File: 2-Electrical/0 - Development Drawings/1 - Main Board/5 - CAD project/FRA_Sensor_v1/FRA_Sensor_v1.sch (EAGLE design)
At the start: 213 parts, among them IC1 CP2101, IC2 ADS1115IDGSR, IC3 P82B715DR, IC4 ADS1115IDGSR, IC5 ADS1115IDGSR, IC8 PCA9555PW, IC9 LDK320ADU50R, J2 ETH_CONN, J3 PJ-059A, J5 WM9734TR-ND, J8 1140084168, J9 + G SCL SDA, Q10 FDN306P, Q11 FDN306P, Q12 FDN306P, Q13 FDN306P, Q14 FDN306P, Q15 FDN306P, Q2 FDN306P, Q3 Si2300DS, Q5 FDN306P, Q6 FDN306P, Q7 DNI, Q8 FDN306P, Q9 FDN306P, T1 BC847, T2 BC847, U1 PCA9509DP, U2 ESP-WROOM-32, X1 TB001-500-02BE, Y3 32.768kHz

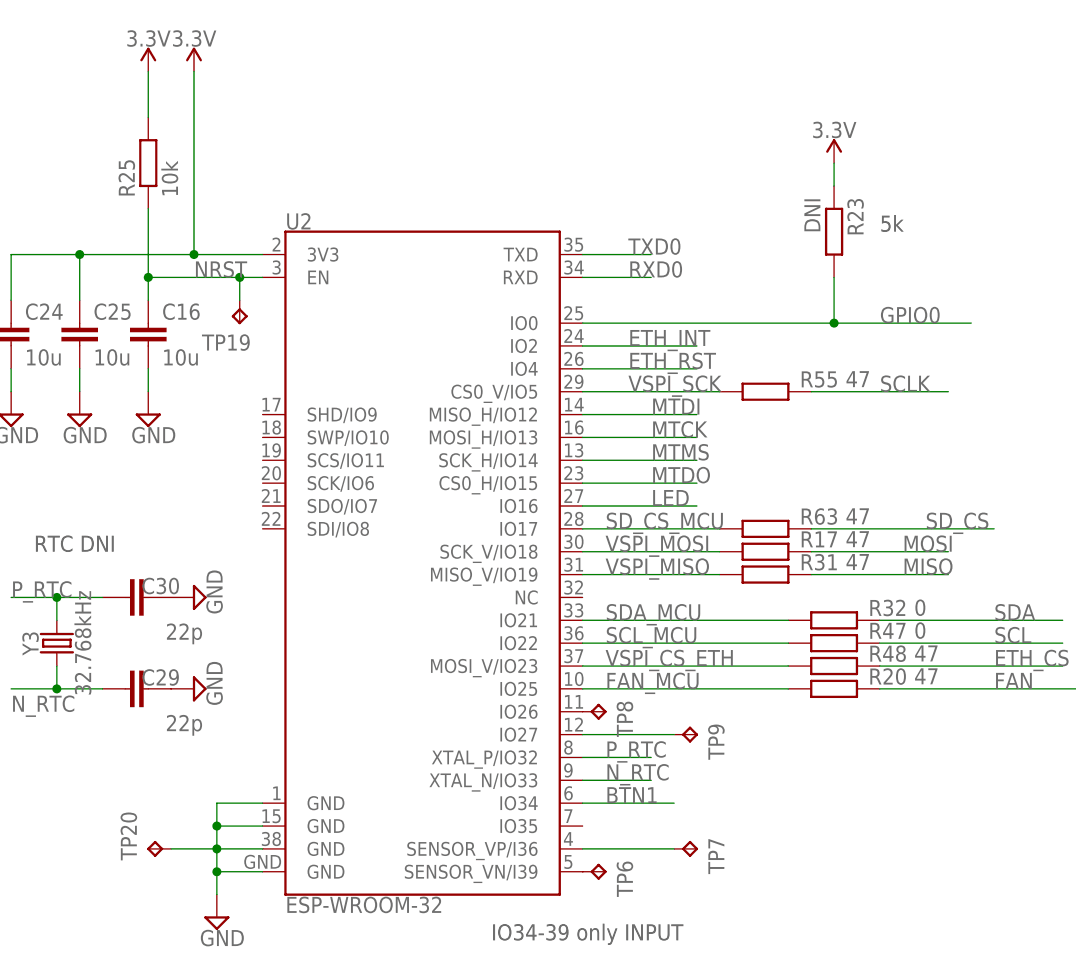
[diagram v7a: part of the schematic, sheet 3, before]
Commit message: error report fixed and sw reset done
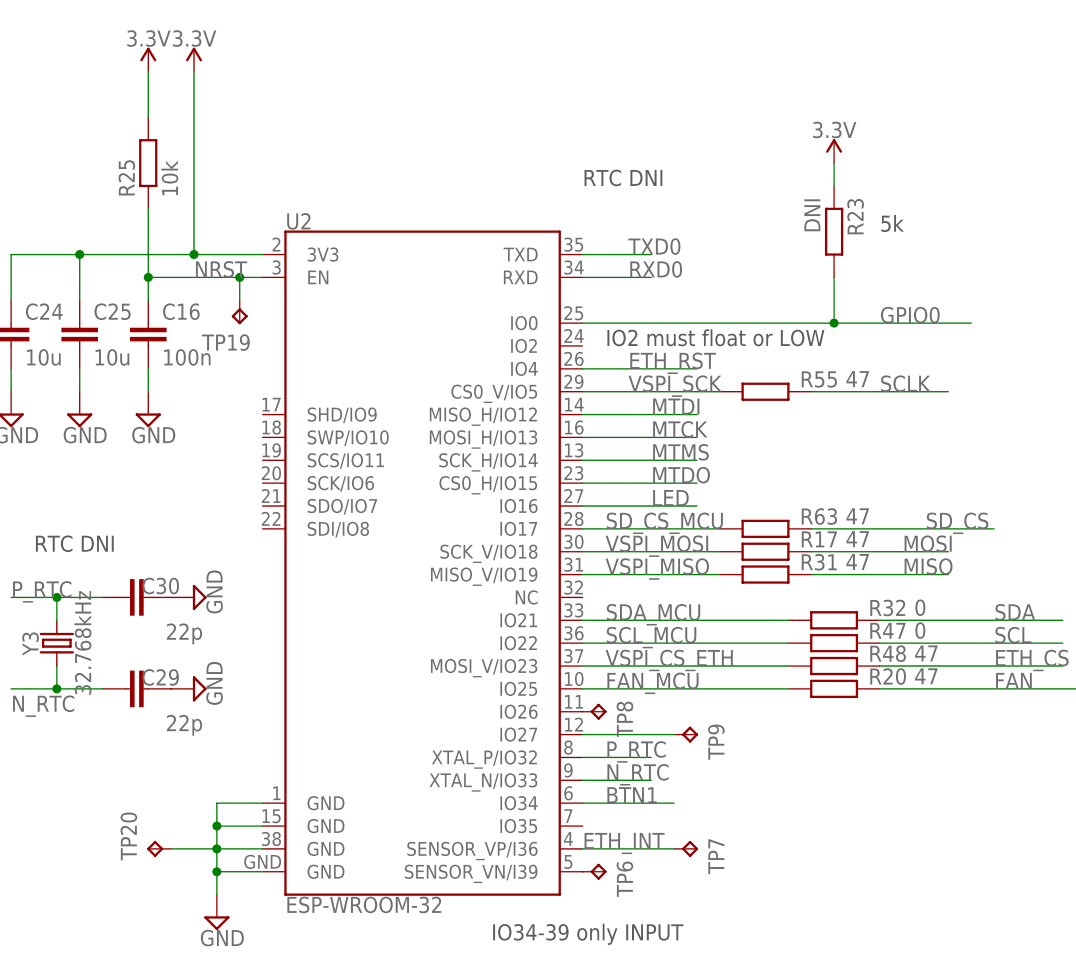
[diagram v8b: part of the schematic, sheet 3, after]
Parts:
- C16: value 10u -> 100n
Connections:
- removed net N$30: TP7.TP, U2.SENSOR_VP/I36
- net ETH_INT: now also TP7.TP, U2.SENSOR_VP/I36; no longer U2.IO2
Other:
- note added: "IO2 must float or LOW"
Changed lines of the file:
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@@
 <grid distance="0.1" unitdist="inch" unit="inch" style="lines" multiple="1" display="no" altdistance="0.01" altunitdist="inch" altunit="inch"/>
 <layers>
-<layer number="1" name="Top" color="4" fill="1" visible="yes" active="no"/>
-<layer number="2" name="Route2" color="1" fill="3" visible="yes" active="no"/>
-<layer number="3" name="Route3" color="4" fill="3" visible="yes" active="no"/>
-<layer number="4" name="Route4" color="1" fill="4" visible="yes" active="no"/>
-<layer number="5" name="Route5" color="4" fill="4" visible="yes" active="no"/>
-<layer number="6" name="Route6" color="1" fill="8" visible="yes" active="no"/>
-<layer number="7" name="Route7" color="4" fill="8" visible="yes" active="no"/>
-<layer number="8" name="Route8" color="1" fill="2" visible="yes" active="no"/>
-<layer number="9" name="Route9" color="4" fill="2" visible="yes" active="no"/>
-<layer number="10" name="Route10" color="1" fill="7" visible="yes" active="no"/>
-<layer number="11" name="Route11" color="4" fill="7" visible="yes" active="no"/>
-<layer number="12" name="Route12" color="1" fill="5" visible="yes" active="no"/>
-<layer number="13" name="Route13" color="4" fill="5" visible="yes" active="no"/>
-<layer number="14" name="Route14" color="1" fill="6" visible="yes" active="no"/>
-<layer number="15" name="Route15" color="4" fill="6" visible="yes" active="no"/>
-<layer number="16" name="Bottom" color="1" fill="1" visible="yes" active="no"/>
-<layer number="17" name="Pads" color="2" fill="1" visible="yes" active="no"/>
-<layer number="18" name="Vias" color="2" fill="1" visible="yes" active="no"/>
-<layer number="19" name="Unrouted" color="6" fill="1" visible="yes" active="no"/>
-<layer number="20" name="Dimension" color="15" fill="1" visible="yes" active="no"/>
-<layer number="21" name="tPlace" color="7" fill="1" visible="yes" active="no"/>
-<layer number="22" name="bPlace" color="7" fill="1" visible="yes" active="no"/>
-<layer number="23" name="tOrigins" color="15" fill="1" visible="yes" active="no"/>
-<layer number="24" name="bOrigins" color="15" fill="1" visible="yes" active="no"/>
-<layer number="25" name="tNames" color="58" fill="1" visible="yes" active="no"/>
-<layer number="26" name="bNames" color="7" fill="1" visible="yes" active="no"/>
-<layer number="27" name="tValues" color="7" fill="1" visible="yes" active="no"/>
-<layer number="28" name="bValues" color="7" fill="1" visible="yes" active="no"/>
+<layer number="1" name="Top" color="4" fill="1" visible="no" active="no"/>
+<layer number="2" name="Route2" color="1" fill="3" visible="no" active="no"/>
+<layer number="3" name="Route3" color="4" fill="3" visible="no" active="no"/>
+<layer number="4" name="Route4" color="1" fill="4" visible="no" active="no"/>
+<layer number="5" name="Route5" color="4" fill="4" visible="no" active="no"/>
+<layer number="6" name="Route6" color="1" fill="8" visible="no" active="no"/>
+<layer number="7" name="Route7" color="4" fill="8" visible="no" active="no"/>
+<layer number="8" name="Route8" color="1" fill="2" visible="no" active="no"/>
+<layer number="9" name="Route9" color="4" fill="2" visible="no" active="no"/>
+<layer number="10" name="Route10" color="1" fill="7" visible="no" active="no"/>
+<layer number="11" name="Route11" color="4" fill="7" visible="no" active="no"/>
+<layer number="12" name="Route12" color="1" fill="5" visible="no" active="no"/>
+<layer number="13" name="Route13" color="4" fill="5" visible="no" active="no"/>
+<layer number="14" name="Route14" color="1" fill="6" visible="no" active="no"/>
+<layer number="15" name="Route15" color="4" fill="6" visible="no" active="no"/>
+<layer number="16" name="Bottom" color="1" fill="1" visible="no" active="no"/>
+<layer number="17" name="Pads" color="2" fill="1" visible="no" active="no"/>
+<layer number="18" name="Vias" color="2" fill="1" visible="no" active="no"/>
+<layer number="19" name="Unrouted" color="6" fill="1" visible="no" active="no"/>
+<layer number="20" name="Dimension" color="15" fill="1" visible="no" active="no"/>
+<layer number="21" name="tPlace" color="7" fill="1" visible="no" active="no"/>
+<layer number="22" name="bPlace" color="7" fill="1" visible="no" active="no"/>
+<layer number="23" name="tOrigins" color="15" fill="1" visible="no" active="no"/>
+<layer number="24" name="bOrigins" color="15" fill="1" visible="no" active="no"/>
+<layer number="25" name="tNames" color="58" fill="1" visible="no" active="no"/>
+<layer number="26" name="bNames" color="7" fill="1" visible="no" active="no"/>
+<layer number="27" name="tValues" color="7" fill="1" visible="no" active="no"/>
+<layer number="28" name="bValues" color="7" fill="1" visible="no" active="no"/>
 <layer number="29" name="tStop" color="7" fill="3" visible="no" active="no"/>
 <layer number="30" name="bStop" color="7" fill="6" visible="no" active="no"/>
@@
 <layer number="35" name="tGlue" color="7" fill="4" visible="no" active="no"/>
 <layer number="36" name="bGlue" color="7" fill="5" visible="no" active="no"/>
-<layer number="37" name="tTest" color="7" fill="1" visible="yes" active="no"/>
-<layer number="38" name="bTest" color="7" fill="1" visible="yes" active="no"/>
+<layer number="37" name="tTest" color="7" fill="1" visible="no" active="no"/>
+<layer number="38" name="bTest" color="7" fill="1" visible="no" active="no"/>
 <layer number="39" name="tKeepout" color="4" fill="11" visible="no" active="no"/>
 <layer number="40" name="bKeepout" color="1" fill="11" visible="no" active="no"/>
@@
 <layer number="44" name="Drills" color="7" fill="1" visible="no" active="no"/>
 <layer number="45" name="Holes" color="7" fill="1" visible="no" active="no"/>
-<layer number="46" name="Milling" color="3" fill="1" visible="yes" active="no"/>
-<layer number="47" name="Measures" color="7" fill="1" visible="yes" active="no"/>
-<layer number="48" name="Document" color="7" fill="1" visible="yes" active="no"/>
-<layer number="49" name="Reference" color="7" fill="1" visible="yes" active="no"/>
-<layer number="50" name="dxf" color="7" fill="1" visible="yes" active="no"/>
-<layer number="51" name="tDocu" color="7" fill="1" visible="yes" active="no"/>
-<layer number="52" name="bDocu" color="7" fill="1" visible="yes" active="no"/>
-<layer number="53" name="tGND_GNDA" color="7" fill="9" visible="yes" active="no"/>
-<layer number="54" name="bGND_GNDA" color="1" fill="9" visible="yes" active="no"/>
-<layer number="56" name="wert" color="7" fill="1" visible="yes" active="no"/>
-<layer number="57" name="tCAD" color="7" fill="1" visible="yes" active="no"/>
-<layer number="59" name="tCarbon" color="7" fill="1" visible="yes" active="no"/>
-<layer number="60" name="bCarbon" color="7" fill="1" visible="yes" active="no"/>
+<layer number="46" name="Milling" color="3" fill="1" visible="no" active="no"/>
+<layer number="47" name="Measures" color="7" fill="1" visible="no" active="no"/>
+<layer number="48" name="Document" color="7" fill="1" visible="no" active="no"/>
+<layer number="49" name="Reference" color="7" fill="1" visible="no" active="no"/>
+<layer number="50" name="dxf" color="7" fill="1" visible="no" active="no"/>
+<layer number="51" name="tDocu" color="7" fill="1" visible="no" active="no"/>
+<layer number="52" name="bDocu" color="7" fill="1" visible="no" active="no"/>
+<layer number="53" name="tGND_GNDA" color="7" fill="9" visible="no" active="no"/>
+<layer number="54" name="bGND_GNDA" color="1" fill="9" visible="no" active="no"/>
+<layer number="56" name="wert" color="7" fill="1" visible="no" active="no"/>
+<layer number="57" name="tCAD" color="7" fill="1" visible="no" active="no"/>
+<layer number="59" name="tCarbon" color="7" fill="1" visible="no" active="no"/>
+<layer number="60" name="bCarbon" color="7" fill="1" visible="no" active="no"/>
 <layer number="88" name="SimResults" color="9" fill="1" visible="yes" active="yes"/>
 <layer number="89" name="SimProbes" color="9" fill="1" visible="yes" active="yes"/>
@@
 <attribute name="PARTNO" value="CRCW060310K0JNEAC"/>
 </part>
-<part name="C16" library="resistor" deviceset="C-EU" device="C0603K" value="10u">
+<part name="C16" library="resistor" deviceset="C-EU" device="C0603K" value="100n">
 <attribute name="PARTNO" value="C0603C102M5RACTU"/>
 </part>
@@
 Mouser GSD090012SEU - not correct</text>
 <text x="106.68" y="86.36" size="1.778" layer="97">5k</text>
+<text x="73.66" y="91.44" size="1.778" layer="97">RTC DNI</text>
+<text x="76.2" y="73.66" size="1.778" layer="97">IO2 must float or LOW</text>
 </plain>
 <instances>
@@
 </segment>
 <segment>
-<pinref part="U2" gate="G$1" pin="IO2"/>
-<wire x1="73.66" y1="73.66" x2="86.36" y2="73.66" width="0.1524" layer="91"/>
-<label x="78.74" y="73.66" size="1.778" layer="95"/>
+<pinref part="U2" gate="G$1" pin="SENSOR_VP/I36"/>
+<pinref part="TP7" gate="G$1" pin="TP"/>
+<wire x1="83.82" y1="17.78" x2="73.66" y2="17.78" width="0.1524" layer="91"/>
+<label x="73.66" y="17.78" size="1.778" layer="95"/>
 </segment>
 </net>
@@
 </segment>
 </net>
-<net name="N$30" class="0">
-<segment>
-<pinref part="U2" gate="G$1" pin="SENSOR_VP/I36"/>
-<pinref part="TP7" gate="G$1" pin="TP"/>
-<wire x1="83.82" y1="17.78" x2="73.66" y2="17.78" width="0.1524" layer="91"/>
-</segment>
-</net>
